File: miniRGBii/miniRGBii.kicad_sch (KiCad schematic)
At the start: 31 parts, among them J1 Conn_01x01_Male, J2 Conn_01x01_Male, J3 Conn_01x01_Male, J4 Conn_01x01_Male, J5 Conn_01x01_Male, J6 Conn_01x01_Male, J7 Conn_01x01_Male, J8 Conn_01x01_Male

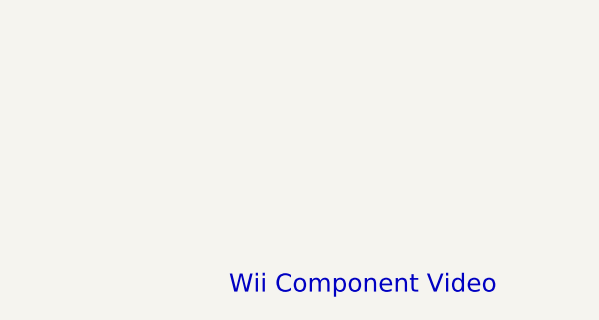
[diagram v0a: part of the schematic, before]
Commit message: That shouldn't have been removed
Signed-off-by: Devnol <pgkoutsoumanis@gmail.com>
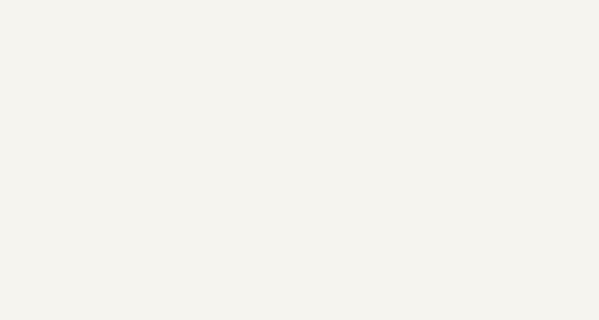
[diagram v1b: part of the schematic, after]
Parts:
- R37, R39, R40: footprint Resistor_SMD:R_0603_1608Metric_Pad1.05x0.95mm_HandSolder -> Resistor_SMD:R_0603_1608Metric_Pad0.98x0.95mm_HandSolder
- gave numbers to parts that had none: 1
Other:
- note removed: "Wii Component Video"
- company: (none) -> Wii mini Hacking
- title: (none) -> miniRGBii Schematic
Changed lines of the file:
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@@
 (kicad_sch (version 20211123) (generator eeschema)
   (paper "A4")
+  (title_block
+    (title "miniRGBii Schematic")
+    (company "Wii mini Hacking")
+    (comment 1 "Devnol")
+    (comment 2 "Job")
+    (comment 3 "Created By:")
+  )
   (junction (at 151.13 69.85) (diameter 0) (color 0 0 0 0)
   )
@@
     (effects (font (size 1.27 1.27)) (justify left bottom))
   )
-  (text "Wii Component Video" (at 187.96 190.5 0)
-    (effects (font (size 2.0066 2.0066)) (justify left bottom))
-  )
   (text "ESD" (at 173.99 26.67 0)
     (effects (font (size 1.27 1.27)) (justify left bottom))
@@
     (property "Reference" "R37" (id 0) (at 135.89 44.45 0))
     (property "Value" "75Ω" (id 1) (at 135.89 46.99 0))
-    (property "Footprint" "Resistor_SMD:R_0603_1608Metric_Pad1.05x0.95mm_HandSolder" (id 2) (at 133.858 45.72 90)
+    (property "Footprint" "Resistor_SMD:R_0603_1608Metric_Pad0.98x0.95mm_HandSolder" (id 2) (at 133.858 45.72 90)
       (effects (font (size 1.27 1.27)) hide)
     )
@@
     (property "Reference" "R39" (id 0) (at 135.89 76.2 0))
     (property "Value" "75Ω" (id 1) (at 135.89 78.74 0))
-    (property "Footprint" "Resistor_SMD:R_0603_1608Metric_Pad1.05x0.95mm_HandSolder" (id 2) (at 130.302 77.47 90)
+    (property "Footprint" "Resistor_SMD:R_0603_1608Metric_Pad0.98x0.95mm_HandSolder" (id 2) (at 130.302 77.47 90)
       (effects (font (size 1.27 1.27)) hide)
     )
@@
     (property "Reference" "R40" (id 0) (at 135.89 106.68 0))
     (property "Value" "75Ω" (id 1) (at 135.89 109.22 0))
-    (property "Footprint" "Resistor_SMD:R_0603_1608Metric_Pad1.05x0.95mm_HandSolder" (id 2) (at 130.302 107.95 90)
+    (property "Footprint" "Resistor_SMD:R_0603_1608Metric_Pad0.98x0.95mm_HandSolder" (id 2) (at 130.302 107.95 90)
       (effects (font (size 1.27 1.27)) hide)
     )
@@
   (symbol (lib_id "Connector:Conn_01x01_Male") (at 24.13 91.44 0) (unit 1)
     (in_bom yes) (on_board yes)
-    (property "Reference" "J?" (id 0) (at 26.8224 89.2302 0)
+    (property "Reference" "J9" (id 0) (at 26.8224 89.2302 0)
       (effects (font (size 1.27 1.27)) hide)
     )
@@
   (symbol (lib_id "power:GND") (at 31.75 93.98 0) (unit 1)
     (in_bom yes) (on_board yes)
-    (property "Reference" "#PWR?" (id 0) (at 31.75 100.33 0)
+    (property "Reference" "#PWR0111" (id 0) (at 31.75 100.33 0)
       (effects (font (size 1.27 1.27)) hide)
     )
@@
     )
     (path "/00000000-0000-0000-0000-00005f077e52"
-      (reference "#PWR?") (unit 1) (value "GND") (footprint "")
+      (reference "#PWR0111") (unit 1) (value "GND") (footprint "")
     )
     (path "/00000000-0000-0000-0000-00005ecd629c"
@@
     )
     (path "/00000000-0000-0000-0000-00005f07713c"
-      (reference "J?") (unit 1) (value "Conn_01x01_Male") (footprint "Pad:pad")
+      (reference "J9") (unit 1) (value "Conn_01x01_Male") (footprint "Pad:pad")
     )
     (path "/00000000-0000-0000-0000-00005ed7acab"
-      (reference "R37") (unit 1) (value "75Ω") (footprint "Resistor_SMD:R_0603_1608Metric_Pad1.05x0.95mm_HandSolder")
+      (reference "R37") (unit 1) (value "75Ω") (footprint "Resistor_SMD:R_0603_1608Metric_Pad0.98x0.95mm_HandSolder")
     )
     (path "/00000000-0000-0000-0000-00005ed7dc27"
-      (reference "R39") (unit 1) (value "75Ω") (footprint "Resistor_SMD:R_0603_1608Metric_Pad1.05x0.95mm_HandSolder")
+      (reference "R39") (unit 1) (value "75Ω") (footprint "Resistor_SMD:R_0603_1608Metric_Pad0.98x0.95mm_HandSolder")
     )
     (path "/00000000-0000-0000-0000-00005ed7ee45"
-      (reference "R40") (unit 1) (value "75Ω") (footprint "Resistor_SMD:R_0603_1608Metric_Pad1.05x0.95mm_HandSolder")
-    )
-  )
+      (reference "R40") (unit 1) (value "75Ω") (footprint "Resistor_SMD:R_0603_1608Metric_Pad0.98x0.95mm_HandSolder")
+    )
+  )
